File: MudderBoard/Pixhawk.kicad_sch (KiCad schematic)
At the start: 0 parts

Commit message: Update Pixhawk.kicad_sch
Updated with pixhawk circuit
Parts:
- added Cff: 33p, GRM1555C1E330JA01D:CAPC1005X55N, symbol Cff:GRM1555C1E330JA01D
- added Cin: 10u, GRM21BR61E106MA73L:CAPC2012X140N, symbol Cin:GRM21BR61E106MA73L
- added CinLDO, CoLDO: 1u, CAPC17595_90N_KEM, symbol CfLDO:C0603C105K8RACTU
- added Cinx: 100n, GRM188R71H104KA93D:CAPC1608X90N, symbol Cinx:GRM188R71H104KA93D
- added Cout: 22u, LMK212BJ226MG-T:CAPC2012X135N, symbol Cout:LMK212BJ226MG-T
- added Coutx: 100n, GRM188R71E104KA01D:CAPC1608X90N, symbol Coutx:GRM188R71E104KA01D
- added L1: 2.2u, XAL5030, symbol L1:XAL5030-222MEB
- added Renb: 14K3, CRCW040214K3FKED:RESC1005X40N, symbol R1:CRCW040214K3FKED
- added Rent: 100K, CRCW0402100KFKED:RESC1005X40N, symbol R2:CRCW0402100KFKED
- added Rfbb: 30K, RES_RC0603_YAG, symbol Rfb2:RC0603FR-0730KL
- added Rfbt: 220K, RC0603FR-07220KL:RESC1607X60N, symbol Rfb1:RC0603FR-07220KL
- added U1: TPS566242DRLR, SOT5x3_DRL_TEX, symbol U1:TPS566242DRLR
- added U2: LP38691DTX-3.3/NOPB, TD03B, symbol U2:LP38691DTX-3.3_NOPB
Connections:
- new net: L1.1, U1.6 (SW)
- new net: Cff.1, Cout.1, Coutx.1, L1.2, Rfbt.1
- new net: Cff.2, Rfbb.1, Rfbt.2, U1.5 (FB)
- new net +BATT: Cin.1, Cinx.1, Rent.1, U1.1 (VIN)
- new net 3V3: CoLDO.1, U2.1 (Vout)
- new net 5V: CinLDO.1, U2.3 (Vin)
- new net EN: Renb.1, Rent.2, U1.2 (EN)
- new net GND1: Cin.2, CinLDO.2, Cinx.2, CoLDO.2, Cout.2, Coutx.2, Renb.2, Rfbb.2, U1.3 (GND), U1.4 (AGND), U2.2 (GND)

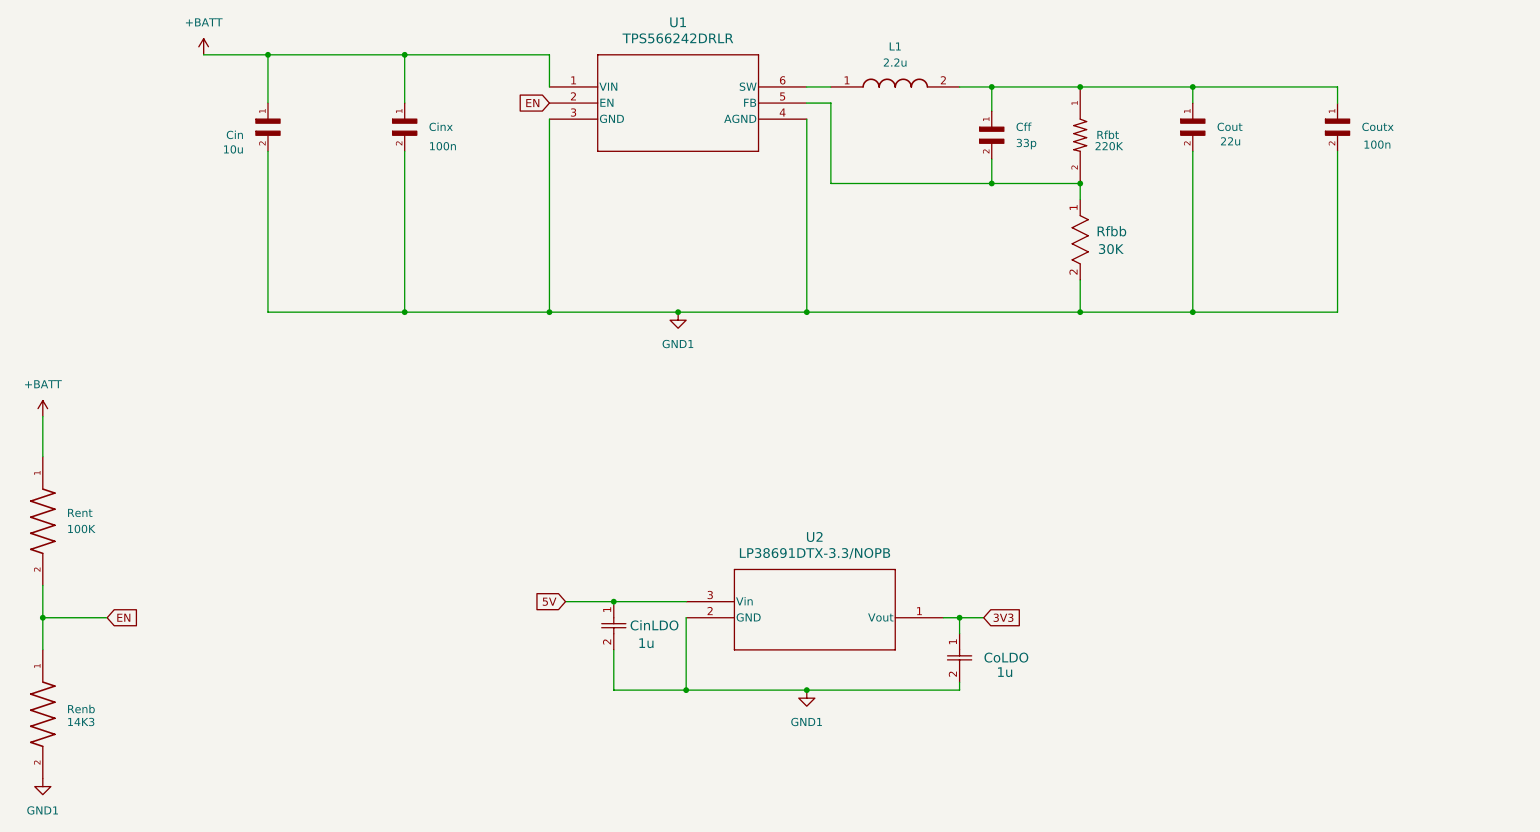
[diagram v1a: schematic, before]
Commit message: Updated Pixhawk Buck
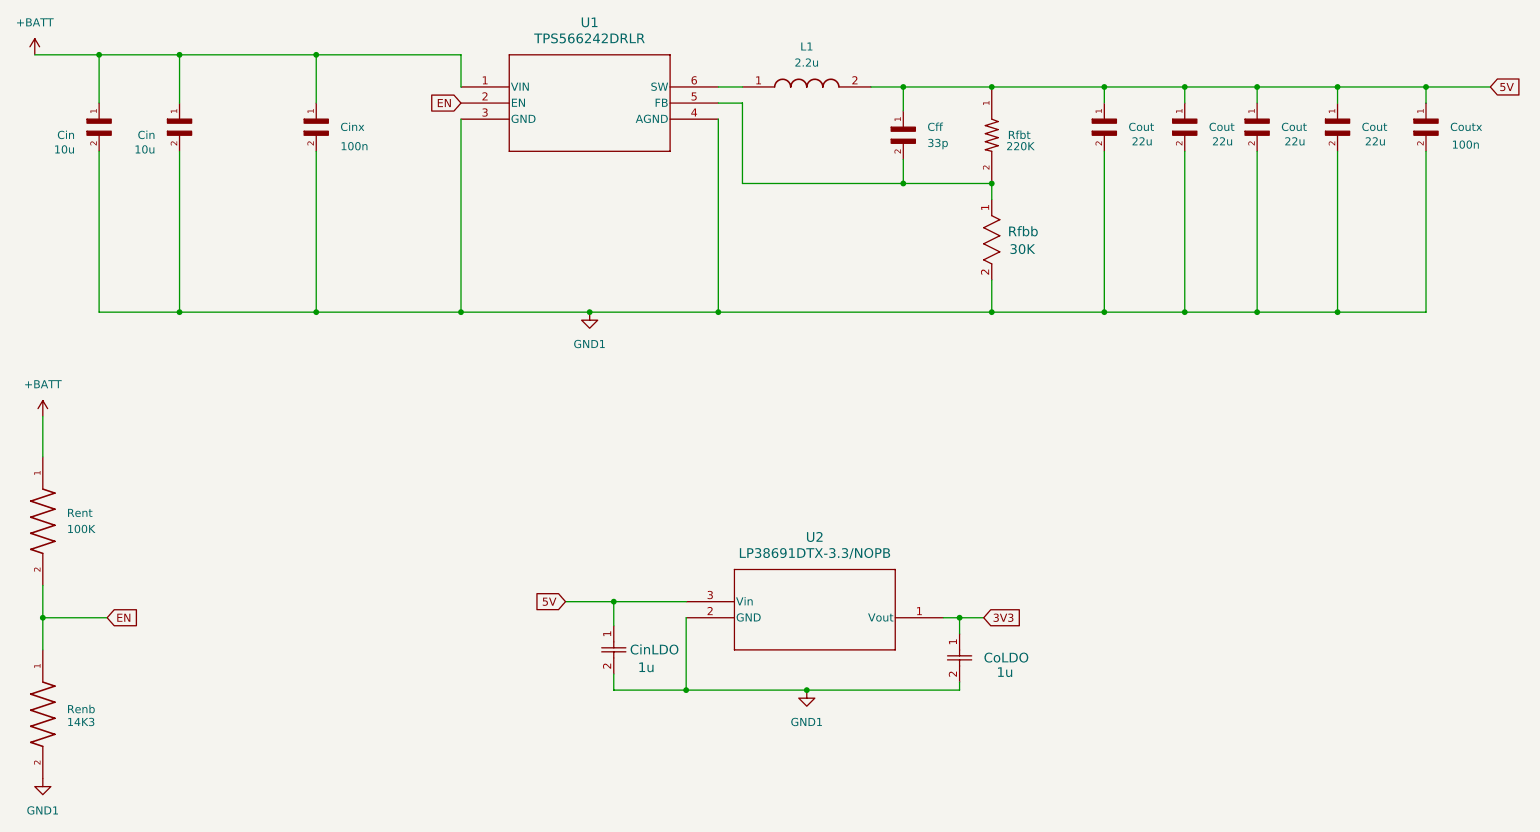
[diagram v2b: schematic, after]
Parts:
- added Cin: 10u, GRM21BR61E106MA73L:CAPC2012X140N, symbol Cin:GRM21BR61E106MA73L
- added Cout (x3): 22u, LMK212BJ226MG-T:CAPC2012X135N, symbol Cout:LMK212BJ226MG-T
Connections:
- net +BATT: now also Cin.1
- net 5V: now also Cff.1, Cout.1, Coutx.1, L1.2, Rfbt.1, Cout.1, Cout.1, Cout.1
- net GND1: now also Cin.2, Cout.2, Cout.2, Cout.2
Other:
- moved on the sheet: Cff, Cin, CinLDO, Cinx, Cout, Coutx, L1, Rfbb, Rfbt, U1

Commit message: added jetson circuit
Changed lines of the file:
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@@
 		(on_board yes)
 		(dnp no)
-		(fields_autoplaced yes)
 		(property "Reference" "#PWR03"
 			(at 39.37 43.18 0)
@@
 		)
 		(property "Value" "+BATT"
-			(at 39.37 34.29 0)
+			(at 37.592 35.56 0)
 			(effects
 				(font
 					(size 1.27 1.27)
 				)
+				(justify left)
 			)
 		)

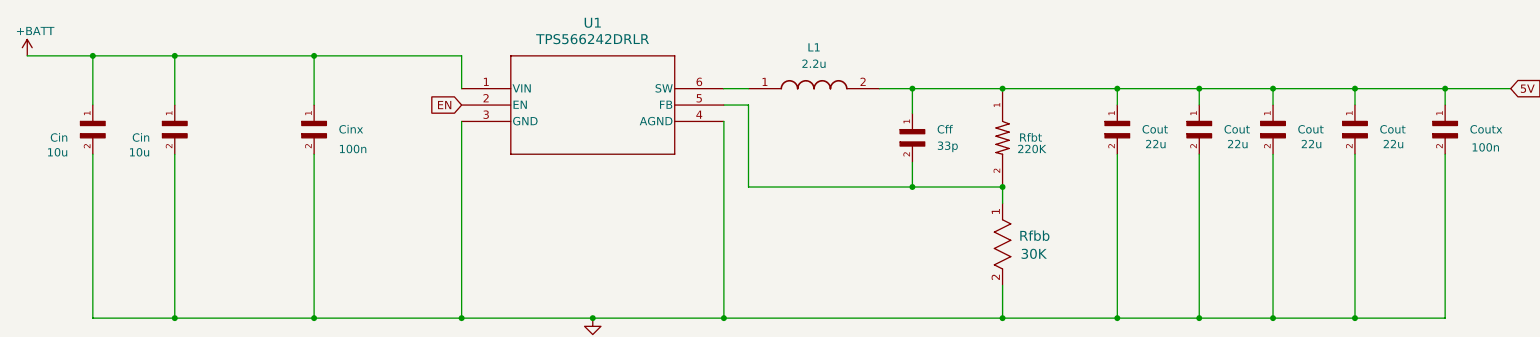
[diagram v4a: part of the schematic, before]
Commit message: added lidar footprints
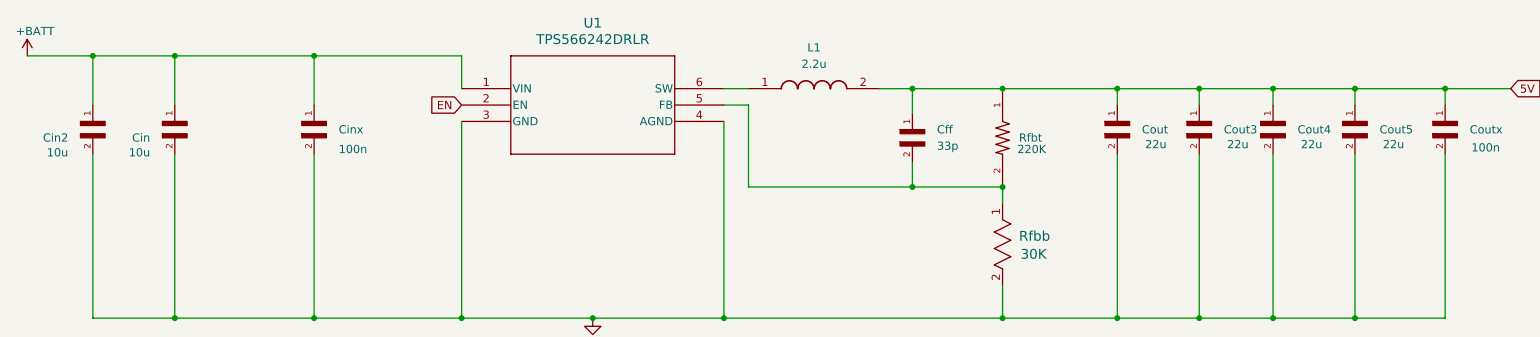
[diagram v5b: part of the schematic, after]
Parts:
- renumbered Cin to Cin2, Cout to Cout3, Cout to Cout4, Cout to Cout5
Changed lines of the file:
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@@
 			(project "MudderBoard"
 				(path "/cdf98bf7-80ce-4b13-b655-e6c7c589c122/0627c6a6-a63c-4c7b-88fc-6e03d8d4f91c"
-					(reference "Cout")
+					(reference "Cout2")
 					(unit 1)
 				)
@@
 			(project "MudderBoard"
 				(path "/cdf98bf7-80ce-4b13-b655-e6c7c589c122/0627c6a6-a63c-4c7b-88fc-6e03d8d4f91c"
-					(reference "Cff")
+					(reference "Cff1")
 					(unit 1)
 				)
@@
 		(on_board yes)
 		(dnp no)
-		(property "Reference" "Cout"
+		(property "Reference" "Cout4"
 			(at 236.22 50.7999 90)
 			(effects
@@
 			(project "MudderBoard"
 				(path "/cdf98bf7-80ce-4b13-b655-e6c7c589c122/0627c6a6-a63c-4c7b-88fc-6e03d8d4f91c"
-					(reference "Cout")
+					(reference "Cout4")
 					(unit 1)
 				)
@@
 			(project "MudderBoard"
 				(path "/cdf98bf7-80ce-4b13-b655-e6c7c589c122/0627c6a6-a63c-4c7b-88fc-6e03d8d4f91c"
-					(reference "Rfbb")
+					(reference "Rfbb2")
 					(unit 1)
 				)
@@
 			(project "MudderBoard"
 				(path "/cdf98bf7-80ce-4b13-b655-e6c7c589c122/0627c6a6-a63c-4c7b-88fc-6e03d8d4f91c"
-					(reference "#PWR05")
+					(reference "#PWR0104")
 					(unit 1)
 				)
@@
 			(project "MudderBoard"
 				(path "/cdf98bf7-80ce-4b13-b655-e6c7c589c122/0627c6a6-a63c-4c7b-88fc-6e03d8d4f91c"
-					(reference "Cinx")
+					(reference "Cinx1")
 					(unit 1)
 				)
@@
 			(project "MudderBoard"
 				(path "/cdf98bf7-80ce-4b13-b655-e6c7c589c122/0627c6a6-a63c-4c7b-88fc-6e03d8d4f91c"
-					(reference "CoLDO")
+					(reference "CoLDO1")
 					(unit 1)
 				)
@@
 			(project "MudderBoard"
 				(path "/cdf98bf7-80ce-4b13-b655-e6c7c589c122/0627c6a6-a63c-4c7b-88fc-6e03d8d4f91c"
-					(reference "#PWR02")
+					(reference "#PWR0101")
 					(unit 1)
 				)
@@
 			(project "MudderBoard"
 				(path "/cdf98bf7-80ce-4b13-b655-e6c7c589c122/0627c6a6-a63c-4c7b-88fc-6e03d8d4f91c"
-					(reference "Cin")
+					(reference "Cin3")
 					(unit 1)
 				)
@@
 			(project "MudderBoard"
 				(path "/cdf98bf7-80ce-4b13-b655-e6c7c589c122/0627c6a6-a63c-4c7b-88fc-6e03d8d4f91c"
-					(reference "#PWR03")
+					(reference "#PWR0103")
 					(unit 1)
 				)
@@
 		(on_board yes)
 		(dnp no)
-		(property "Reference" "Cin"
+		(property "Reference" "Cin2"
 			(at 45.72 52.0701 90)
 			(effects
@@
 			(project "MudderBoard"
 				(path "/cdf98bf7-80ce-4b13-b655-e6c7c589c122/0627c6a6-a63c-4c7b-88fc-6e03d8d4f91c"
-					(reference "Cin")
+					(reference "Cin2")
 					(unit 1)
 				)
@@
 			(project "MudderBoard"
 				(path "/cdf98bf7-80ce-4b13-b655-e6c7c589c122/0627c6a6-a63c-4c7b-88fc-6e03d8d4f91c"
-					(reference "Rfbt")
+					(reference "Rfbt1")
 					(unit 1)
 				)
@@
 			(project "MudderBoard"
 				(path "/cdf98bf7-80ce-4b13-b655-e6c7c589c122/0627c6a6-a63c-4c7b-88fc-6e03d8d4f91c"
-					(reference "#PWR01")
+					(reference "#PWR0102")
 					(unit 1)
 				)
@@
 			(project "MudderBoard"
 				(path "/cdf98bf7-80ce-4b13-b655-e6c7c589c122/0627c6a6-a63c-4c7b-88fc-6e03d8d4f91c"
-					(reference "Rent")
+					(reference "Rent1")
 					(unit 1)
 				)
@@
 			(project "MudderBoard"
 				(path "/cdf98bf7-80ce-4b13-b655-e6c7c589c122/0627c6a6-a63c-4c7b-88fc-6e03d8d4f91c"
-					(reference "Coutx")
+					(reference "Coutx1")
 					(unit 1)
 				)
@@
 		(on_board yes)
 		(dnp no)
-		(property "Reference" "Cout"
+		(property "Reference" "Cout3"
 			(at 224.79 50.7999 90)
 			(effects
@@
 			(project "MudderBoard"
 				(path "/cdf98bf7-80ce-4b13-b655-e6c7c589c122/0627c6a6-a63c-4c7b-88fc-6e03d8d4f91c"
-					(reference "Cout")
+					(reference "Cout3")
 					(unit 1)
 				)
@@
 			(project "MudderBoard"
 				(path "/cdf98bf7-80ce-4b13-b655-e6c7c589c122/0627c6a6-a63c-4c7b-88fc-6e03d8d4f91c"
-					(reference "CinLDO")
+					(reference "CinLDO1")
 					(unit 1)
 				)
@@
 			(project "MudderBoard"
 				(path "/cdf98bf7-80ce-4b13-b655-e6c7c589c122/0627c6a6-a63c-4c7b-88fc-6e03d8d4f91c"
-					(reference "Renb")
+					(reference "Renb1")
 					(unit 1)
 				)
@@
 		(on_board yes)
 		(dnp no)
-		(property "Reference" "Cout"
+		(property "Reference" "Cout5"
 			(at 248.92 50.7999 90)
 			(effects
@@
 			(project "MudderBoard"
 				(path "/cdf98bf7-80ce-4b13-b655-e6c7c589c122/0627c6a6-a63c-4c7b-88fc-6e03d8d4f91c"
-					(reference "Cout")
+					(reference "Cout5")
 					(unit 1)
 				)
@@
 			(project "MudderBoard"
 				(path "/cdf98bf7-80ce-4b13-b655-e6c7c589c122/0627c6a6-a63c-4c7b-88fc-6e03d8d4f91c"
-					(reference "#PWR04")
-					(unit 1)
-				)
+					(reference "#PWR0105")
+					(unit 1)
+				)

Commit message: added pixhawk footprints
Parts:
- Cff: footprint GRM1555C1E330JA01D:CAPC1005X55N -> PH_Foot:CAPC1005X55N
- Cin, Cin2: footprint GRM21BR61E106MA73L:CAPC2012X140N -> PH_Foot:CAPC2012X140N
- CinLDO, CoLDO: footprint CAPC17595_90N_KEM -> PH_Foot:CAPC1608X90N
- Cinx: footprint GRM188R71H104KA93D:CAPC1608X90N -> PH_Foot:CAPC1608X90N
- Cout, Cout3, Cout4, Cout5: footprint LMK212BJ226MG-T:CAPC2012X135N -> PH_Foot:CAPC2012X135N
- Coutx: footprint GRM188R71E104KA01D:CAPC1608X90N -> PH_Foot:CAPC1608X90N
- L1: footprint XAL5030 -> PH_Foot:XAL5030222MEC
- Renb: footprint CRCW040214K3FKED:RESC1005X40N -> PH_Foot:RESC1005X40N
- Rent: footprint CRCW0402100KFKED:RESC1005X40N -> PH_Foot:RESC1005X40N
- Rfbb: footprint RES_RC0603_YAG -> PH_Foot:R0603
- Rfbt: footprint RC0603FR-07220KL:RESC1607X60N -> PH_Foot:RESC1607X60N
- U1: footprint SOT5x3_DRL_TEX -> PH_Foot:SOT5x3_DRL_TEX
- U2: footprint TD03B -> PH_Foot:TO228P1042X238-3N
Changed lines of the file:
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@@
 			)
 		)
-		(property "Footprint" "XAL5030"
+		(property "Footprint" "PH_Foot:XAL5030222MEC"
 			(at 167.64 140.64 0)
 			(effects
@@
 			)
 		)
-		(property "Footprint" "LMK212BJ226MG-T:CAPC2012X135N"
+		(property "Footprint" "PH_Foot:CAPC2012X135N"
 			(at 208.28 49.53 0)
 			(effects
@@
 			)
 		)
-		(property "Footprint" "GRM1555C1E330JA01D:CAPC1005X55N"
+		(property "Footprint" "PH_Foot:CAPC1005X55N"
 			(at 176.53 50.8 0)
 			(effects
@@
 			)
 		)
-		(property "Footprint" "LMK212BJ226MG-T:CAPC2012X135N"
+		(property "Footprint" "PH_Foot:CAPC2012X135N"
 			(at 232.41 49.53 0)
 			(effects
@@
 			)
 		)
-		(property "Footprint" "RES_RC0603_YAG"
+		(property "Footprint" "PH_Foot:R0603"
 			(at 190.5 62.23 0)
 			(effects
@@
 			)
 		)
-		(property "Footprint" "GRM188R71H104KA93D:CAPC1608X90N"
+		(property "Footprint" "PH_Foot:CAPC1608X90N"
 			(at 83.82 49.53 0)
 			(effects
@@
 			)
 		)
-		(property "Footprint" "CAPC17595_90N_KEM"
+		(property "Footprint" "PH_Foot:CAPC1608X90N"
 			(at 185.42 130.81 0)
 			(effects
@@
 			)
 		)
-		(property "Footprint" "GRM21BR61E106MA73L:CAPC2012X140N"
+		(property "Footprint" "PH_Foot:CAPC2012X140N"
 			(at 62.23 49.53 0)
 			(effects
@@
 			)
 		)
-		(property "Footprint" "TD03B"
+		(property "Footprint" "PH_Foot:TO228P1042X238-3N"
 			(at 182.88 128.27 0)
 			(effects
@@
 			)
 		)
-		(property "Footprint" "GRM21BR61E106MA73L:CAPC2012X140N"
+		(property "Footprint" "PH_Foot:CAPC2012X140N"
 			(at 49.53 49.53 0)
 			(effects
@@
 			)
 		)
-		(property "Footprint" "RC0603FR-07220KL:RESC1607X60N"
+		(property "Footprint" "PH_Foot:RESC1607X60N"
 			(at 190.5 52.07 0)
 			(effects
@@
 			)
 		)
-		(property "Footprint" "SOT5x3_DRL_TEX"
+		(property "Footprint" "PH_Foot:SOT5x3_DRL_TEX"
 			(at 104.648 35.814 0)
 			(effects
@@
 			)
 		)
-		(property "Footprint" "CRCW0402100KFKED:RESC1005X40N"
+		(property "Footprint" "PH_Foot:RESC1005X40N"
 			(at 40.64 113.03 0)
 			(effects
@@
 			)
 		)
-		(property "Footprint" "GRM188R71E104KA01D:CAPC1608X90N"
+		(property "Footprint" "PH_Foot:CAPC1608X90N"
 			(at 259.08 49.53 0)
 			(effects
@@
 			)
 		)
-		(property "Footprint" "LMK212BJ226MG-T:CAPC2012X135N"
+		(property "Footprint" "PH_Foot:CAPC2012X135N"
 			(at 220.98 49.53 0)
 			(effects
@@
 			)
 		)
-		(property "Footprint" "CAPC17595_90N_KEM"
+		(property "Footprint" "PH_Foot:CAPC1608X90N"
 			(at 130.81 129.54 0)
 			(effects
@@
 			)
 		)
-		(property "Footprint" "CRCW040214K3FKED:RESC1005X40N"
+		(property "Footprint" "PH_Foot:RESC1005X40N"
 			(at 40.64 143.51 0)
 			(effects
@@
 			)
 		)
-		(property "Footprint" "LMK212BJ226MG-T:CAPC2012X135N"
+		(property "Footprint" "PH_Foot:CAPC2012X135N"
 			(at 245.11 49.53 0)
 			(effects
